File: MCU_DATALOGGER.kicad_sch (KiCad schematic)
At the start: 25 parts, among them U1 24LC1025, U2 24LC1025, U3 DS1337S_, U4 ATMEGA328P-AU, Y2 Crystal, Y3 Crystal

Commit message: Associated all footprints to the symbols
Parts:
- C1, C4: value C -> 0.1uF; footprint (none) -> Capacitor_SMD:C_0805_2012Metric
- C2, C3: value C -> 22pF; footprint (none) -> Capacitor_SMD:C_0805_2012Metric
- C5: value C_Polarized -> 100nF; footprint (none) -> Capacitor_SMD:C_0805_2012Metric
- D1, D2: footprint (none) -> LED_SMD:LED_0805_2012Metric
- H1, H2, H3, H4: footprint (none) -> MountingHole:MountingHole_2.1mm
- R1, R2, R6: value R -> 10K; footprint (none) -> Resistor_SMD:R_0805_2012Metric
- R3, R4: value R -> 4.7K; footprint (none) -> Resistor_SMD:R_0805_2012Metric
- R5, R7: value R -> 330; footprint (none) -> Resistor_SMD:R_0805_2012Metric
- U1, U2: footprint (none) -> Package_SO:SOIC-8_5.3x5.3mm_P1.27mm
- Y1: renamed from Y3; value Crystal -> 32.768 KHz; footprint (none) -> Crystal:Crystal_SMD_5032-2Pin_5.0x3.2mm_HandSoldering
- Y2: value Crystal -> 16 MHz; footprint (none) -> Crystal:Crystal_SMD_5032-2Pin_5.0x3.2mm_HandSoldering
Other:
- moved on the sheet: C1, R1, R2, U3

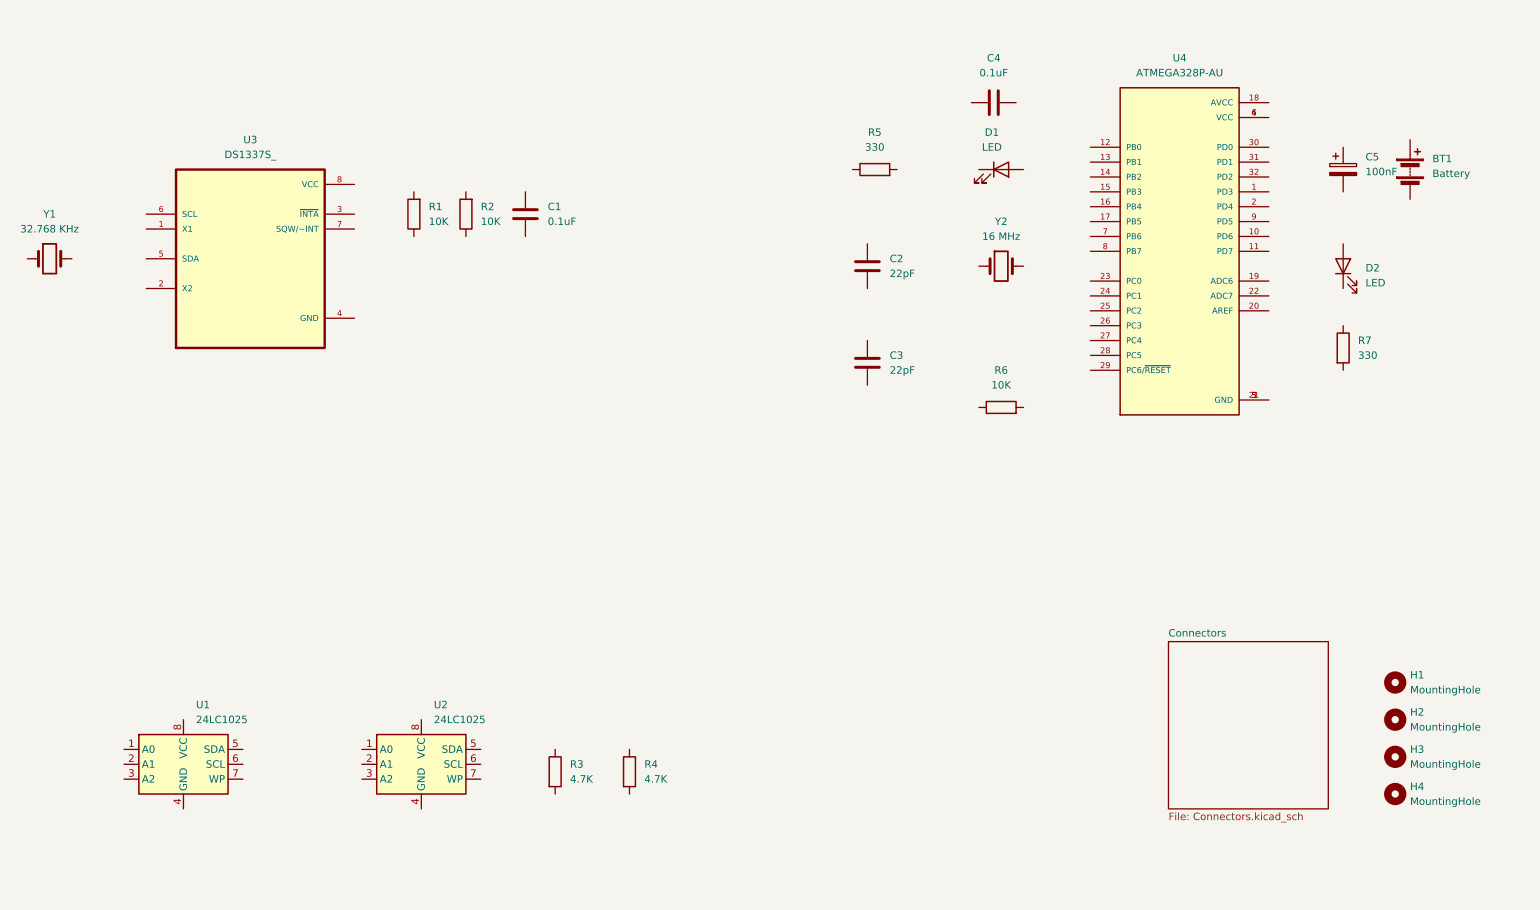
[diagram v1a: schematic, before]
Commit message: Wired all symbols in the schematics sheet 1
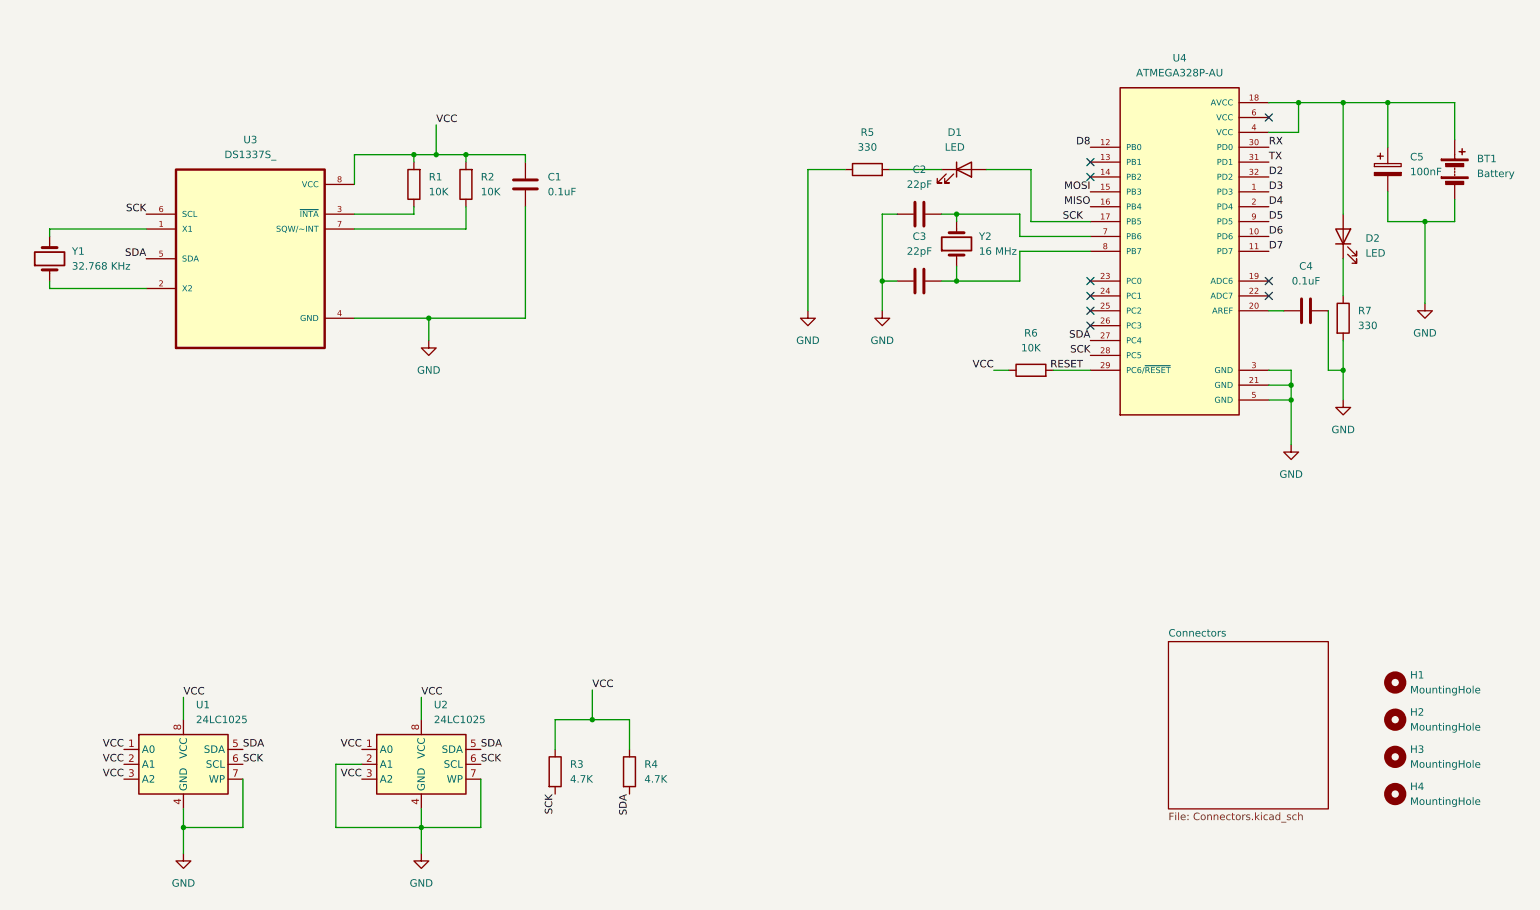
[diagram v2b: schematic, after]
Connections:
- net VCC: now reaches R3.1
- net VCC: now also C1.2, R1.2, R2.2, R4.1, R6.1, U1.1 (A0), U1.2 (A1), U1.3 (A2), U1.8 (VCC), U2.1 (A0), U2.3 (A2), U2.8 (VCC), U3.8 (VCC)
- net SCK: now reaches R3.2
- net SCK: now also D1.2 (A), U1.6 (SCL), U2.6 (SCL), U3.6 (SCL), U4.17 (PB5), U4.28 (PC5)
- net at R1.1: now also U3.3 (~{INTA})
- net SDA: now reaches R4.2
- net SDA: now also U1.5 (SDA), U2.5 (SDA), U3.5 (SDA), U4.27 (PC4)
- net D3: now reaches U4.1 (PD3)
- net D6: now reaches U4.10 (PD6)
- net D7: now reaches U4.11 (PD7)
- net D8: now reaches U4.12 (PB0)
- net MOSI: now reaches U4.15 (PB3)
- net MISO: now reaches U4.16 (PB4)
- net at U4.18 (AVCC): now also BT1.1 (+), C5.1, D2.2 (A), U4.4 (VCC)
- net D4: now reaches U4.2 (PD4)
- net at U4.20 (AREF): now also C4.1
- net GND: now reaches U4.21 (GND), U4.3 (GND), U4.5 (GND)
- net GND: now also BT1.2 (-), C1.1, C2.2, C3.1, C4.2, C5.2, R5.1, R7.2, U1.4 (GND), U1.7 (WP), U2.2 (A1), U2.4 (GND), U2.7 (WP), U3.4 (GND)
- net RESET: now reaches U4.29 (PC6/~{RESET})
- net RESET: now also R6.2
- net RX: now reaches U4.30 (PD0)
- net TX: now reaches U4.31 (PD1)
- net D2: now reaches U4.32 (PD2)
- net at U4.6 (VCC): no longer U4.4 (VCC)
- net at U4.7 (PB6): now also C2.1, Y2.2
- net at U4.8 (PB7): now also C3.2, Y2.1
- net D5: now reaches U4.9 (PD5)
- net at R5.2: now also D1.1 (K)
- net at Y1.1: now also U3.2 (X2)
- net at Y1.2: now also U3.1 (X1)
- net at U3.7 (SQW/~INT): now also R2.1
- net at R7.1: now also D2.1 (K)
- no-connect marks 0 -> 9
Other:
- moved on the sheet: BT1, C1, C2, C3, C4, C5, D1, D2, R1, R2, R5, R6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

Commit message: Net classes is added
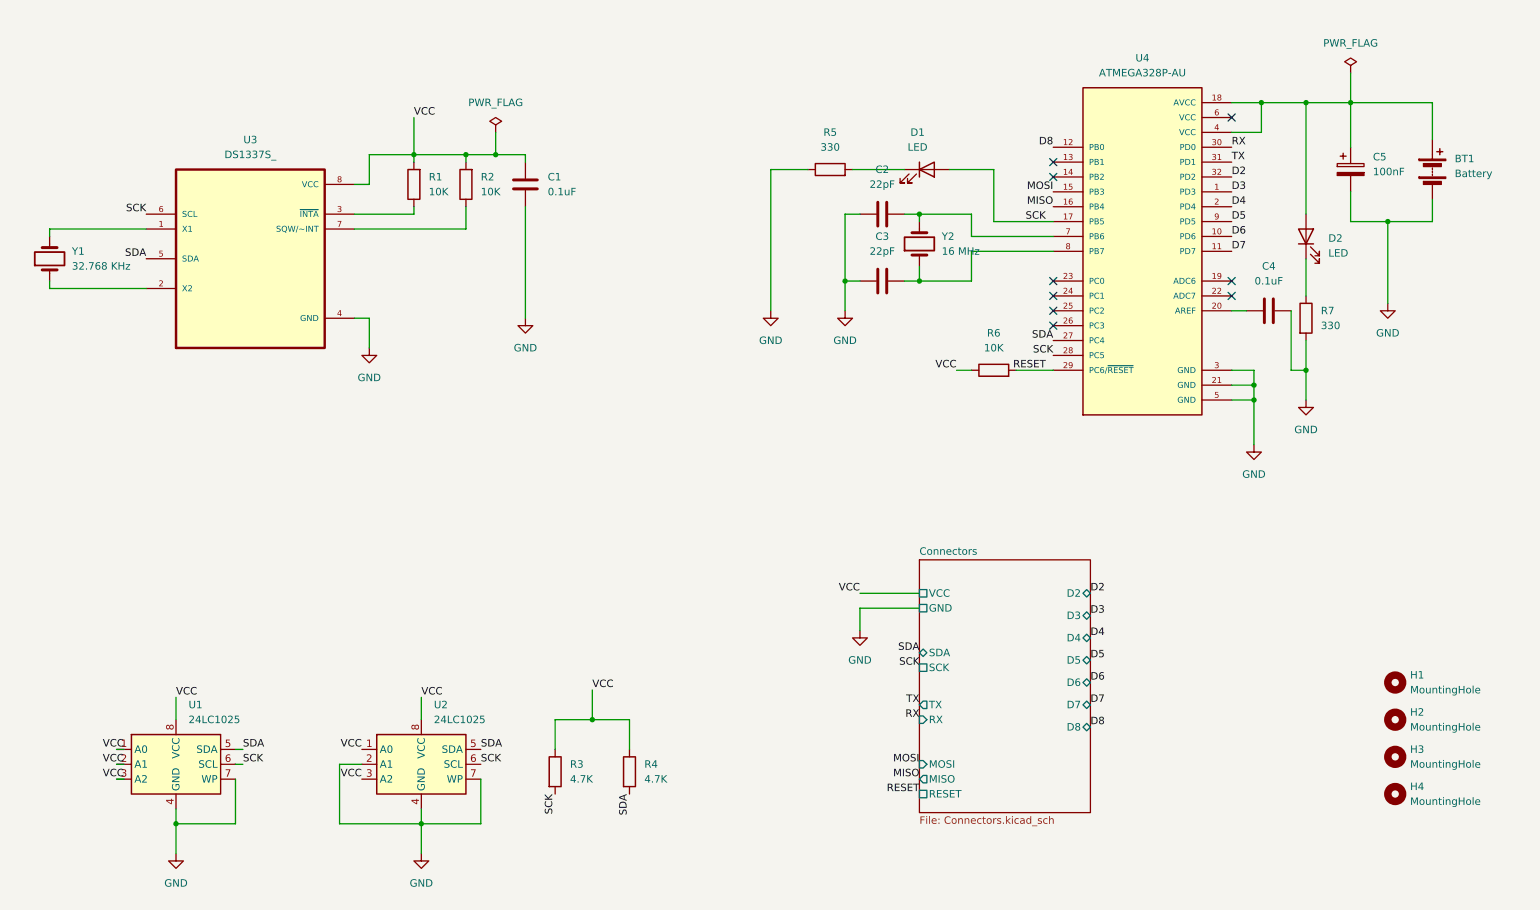
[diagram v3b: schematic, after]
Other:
- sheet Connectors ports: added D2, D3, D4, D5, D6, D7, D8, GND, MISO, MOSI, RESET, RX, SCK, SDA, TX, VCC; removed none
- moved on the sheet: BT1, C2, C3, C4, C5, D1, D2, R5, R6, R7, U1, U4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

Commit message: Added comments to schematics
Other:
- note added: "EEPROM"
- note added: "MCU"
- note added: "Mounting Holes"
- note added: "Real Time Clock"
- moved on the sheet: H1, H2, H3, H4
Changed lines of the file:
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@@
 		(rev "1.0")
 	)
+	(rectangle
+		(start 245.745 125.095)
+		(end 266.7 154.305)
+		(stroke
+			(width 0)
+			(type default)
+		)
+		(fill
+			(type none)
+		)
+	)
+	(rectangle
+		(start 33.655 34.29)
+		(end 128.905 86.36)
+		(stroke
+			(width 0)
+			(type default)
+		)
+		(fill
+			(type none)
+		)
+	)
+	(rectangle
+		(start 157.48 24.765)
+		(end 284.48 102.235)
+		(stroke
+			(width 0)
+			(type default)
+		)
+		(fill
+			(type none)
+		)
+	)
+	(rectangle
+		(start 43.815 133.35)
+		(end 144.145 172.72)
+		(stroke
+			(width 0)
+			(type default)
+		)
+		(fill
+			(type none)
+		)
+	)
+	(text "MCU"
+		(exclude_from_sim no)
+		(at 160.02 22.86 0)
+		(effects
+			(font
+				(size 1.27 1.27)
+			)
+		)
+	)
+	(text "EEPROM"
+		(exclude_from_sim no)
+		(at 48.26 132.08 0)
+		(effects
+			(font
+				(size 1.27 1.27)
+			)
+		)
+	)
+	(text "Mounting Holes"
+		(exclude_from_sim no)
+		(at 252.73 123.19 0)
+		(effects
+			(font
+				(size 1.27 1.27)
+			)
+		)
+	)
+	(text "Real Time Clock"
+		(exclude_from_sim no)
+		(at 41.91 33.02 0)
+		(effects
+			(font
+				(size 1.27 1.27)
+			)
+		)
+	)
 	(junction
 		(at 259.08 36.83)
@@
 	(symbol
 		(lib_id "Mechanical:MountingHole")
-		(at 266.7 135.89 0)
+		(at 250.19 130.81 0)
 		(unit 1)
 		(exclude_from_sim no)
@@
 		(fields_autoplaced yes)
 		(property "Reference" "H1"
-			(at 269.24 134.6199 0)
+			(at 252.73 129.5399 0)
 			(effects
 				(font
@@
 		)
 		(property "Value" "MountingHole"
-			(at 269.24 137.1599 0)
+			(at 252.73 132.0799 0)
 			(effects
 				(font
@@
 		)
 		(property "Footprint" "MountingHole:MountingHole_2.1mm"
-			(at 266.7 135.89 0)
+			(at 250.19 130.81 0)
 			(effects
 				(font
@@
 		)
 		(property "Datasheet" "~"
-			(at 266.7 135.89 0)
+			(at 250.19 130.81 0)
 			(effects
 				(font
@@
 		)
 		(property "Description" "Mounting Hole without connection"
-			(at 266.7 135.89 0)
+			(at 250.19 130.81 0)
 			(effects
 				(font
@@
 	(symbol
 		(lib_id "Mechanical:MountingHole")
-		(at 266.7 154.94 0)
+		(at 250.19 149.86 0)
 		(unit 1)
 		(exclude_from_sim no)
@@
 		(fields_autoplaced yes)
 		(property "Reference" "H4"
-			(at 269.24 153.6699 0)
+			(at 252.73 148.5899 0)
 			(effects
 				(font
@@
 		)
 		(property "Value" "MountingHole"
-			(at 269.24 156.2099 0)
+			(at 252.73 151.1299 0)
 			(effects
 				(font
@@
 		)
 		(property "Footprint" "MountingHole:MountingHole_2.1mm"
-			(at 266.7 154.94 0)
+			(at 250.19 149.86 0)
 			(effects
 				(font
@@
 		)
 		(property "Datasheet" "~"
-			(at 266.7 154.94 0)
+			(at 250.19 149.86 0)
 			(effects
 				(font
@@
 		)
 		(property "Description" "Mounting Hole without connection"
-			(at 266.7 154.94 0)
+			(at 250.19 149.86 0)
 			(effects
 				(font
@@
 	(symbol
 		(lib_id "Mechanical:MountingHole")
-		(at 266.7 148.59 0)
+		(at 250.19 143.51 0)
 		(unit 1)
 		(exclude_from_sim no)
@@
 		(fields_autoplaced yes)
 		(property "Reference" "H3"
-			(at 269.24 147.3199 0)
+			(at 252.73 142.2399 0)
 			(effects
 				(font
@@
 		)
 		(property "Value" "MountingHole"
-			(at 269.24 149.8599 0)
+			(at 252.73 144.7799 0)
 			(effects
 				(font
@@
 		)
 		(property "Footprint" "MountingHole:MountingHole_2.1mm"
-			(at 266.7 148.59 0)
+			(at 250.19 143.51 0)
 			(effects
 				(font
@@
 		)
 		(property "Datasheet" "~"
-			(at 266.7 148.59 0)
+			(at 250.19 143.51 0)
 			(effects
 				(font
@@
 		)
 		(property "Description" "Mounting Hole without connection"
-			(at 266.7 148.59 0)
+			(at 250.19 143.51 0)
 			(effects
 				(font
@@
 	(symbol
 		(lib_id "Mechanical:MountingHole")
-		(at 266.7 142.24 0)
+		(at 250.19 137.16 0)
 		(unit 1)
 		(exclude_from_sim no)
@@
 		(fields_autoplaced yes)
 		(property "Reference" "H2"
-			(at 269.24 140.9699 0)
+			(at 252.73 135.8899 0)
 			(effects
 				(font
@@
 		)
 		(property "Value" "MountingHole"
-			(at 269.24 143.5099 0)
+			(at 252.73 138.4299 0)
 			(effects
 				(font
@@
 		)
 		(property "Footprint" "MountingHole:MountingHole_2.1mm"
-			(at 266.7 142.24 0)
+			(at 250.19 137.16 0)
 			(effects
 				(font
@@
 		)
 		(property "Datasheet" "~"
-			(at 266.7 142.24 0)
+			(at 250.19 137.16 0)
 			(effects
 				(font
@@
 		)
 		(property "Description" "Mounting Hole without connection"
-			(at 266.7 142.24 0)
+			(at 250.19 137.16 0)
 			(effects
 				(font

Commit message: Added & arranged footprints
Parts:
- BT1: footprint (none) -> Connector_PinHeader_2.54mm:PinHeader_1x02_P2.54mm_Vertical
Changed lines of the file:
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@@
 			)
 		)
-		(property "Footprint" ""
+		(property "Footprint" "Connector_PinHeader_2.54mm:PinHeader_1x02_P2.54mm_Vertical"
 			(at 273.05 46.736 90)
 			(effects

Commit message: Completed layout design of 2 layer
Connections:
- net VCC: now also BT1.1 (+), C5.1, D2.2 (A), U4.18 (AVCC), U4.4 (VCC)
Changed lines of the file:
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@@
+	)
+	(label "VCC"
+		(at 273.05 36.83 0)
+		(effects
+			(font
+				(size 1.27 1.27)
+			)
+			(justify left bottom)
+		)
 	)
 	(label "VCC"
